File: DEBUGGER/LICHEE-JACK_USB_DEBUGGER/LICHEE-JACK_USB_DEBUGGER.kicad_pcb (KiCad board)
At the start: 2 copper layers, 45 x 20 mm, 52 parts, among them Q1 AO3401A, U1 USB2422/MJ, U3 TPSPX3819M5-L-3-3, U4 CP2102-GMR, X1 XL7EL89CMI-111YLC-24M

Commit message: replace some obj
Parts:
- removed LED3: LED_ORANGE/YELLOW_TXD, YLED0603O:LED0603-FD
- added LED5: LED_YELLOW_RXD, YLED0603G:LED0603-FD, F.Cu at (145.0, 63.0)
- added TP4: TP_VBUS, TestPoint:TestPoint_Pad_D1.0mm, B.Cu at (144.6, 71.2)
- added TP5: TP_GND, TestPoint:TestPoint_Pad_D1.0mm, B.Cu at (147.3, 71.2)
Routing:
- net GNDREF: track 153.9 -> 157.6 mm
- net VBUS: track 66.3 -> 68.3 mm

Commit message: rename LED5
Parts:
- renumbered LED5 to LED3
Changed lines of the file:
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@@
 	(net 58 "GNDREF")
 	(net 59 "Net-(D8-Pad2)")
-	(net 60 "Net-(LED5--)")
+	(net 60 "Net-(LED3--)")
 	(footprint "Capacitor_SMD:C_0402_1005Metric"
 		(layer "F.Cu")
@@
 			(layers "F.Cu" "F.Mask" "F.Paste")
 			(roundrect_rratio 0.25)
-			(net 60 "Net-(LED5--)")
+			(net 60 "Net-(LED3--)")
 			(pintype "passive")
 		)
@@
 		(layer "F.Cu")
 		(at 145 63 90)
-		(property "Reference" "LED5"
+		(property "Reference" "LED3"
 			(at 0 -4 90)
 			(layer "F.SilkS")
@@
 			(size 1 0.9)
 			(layers "F.Cu" "F.Mask" "F.Paste")
-			(net 60 "Net-(LED5--)")
+			(net 60 "Net-(LED3--)")
 			(pinfunction "-")
 			(pintype "unspecified")

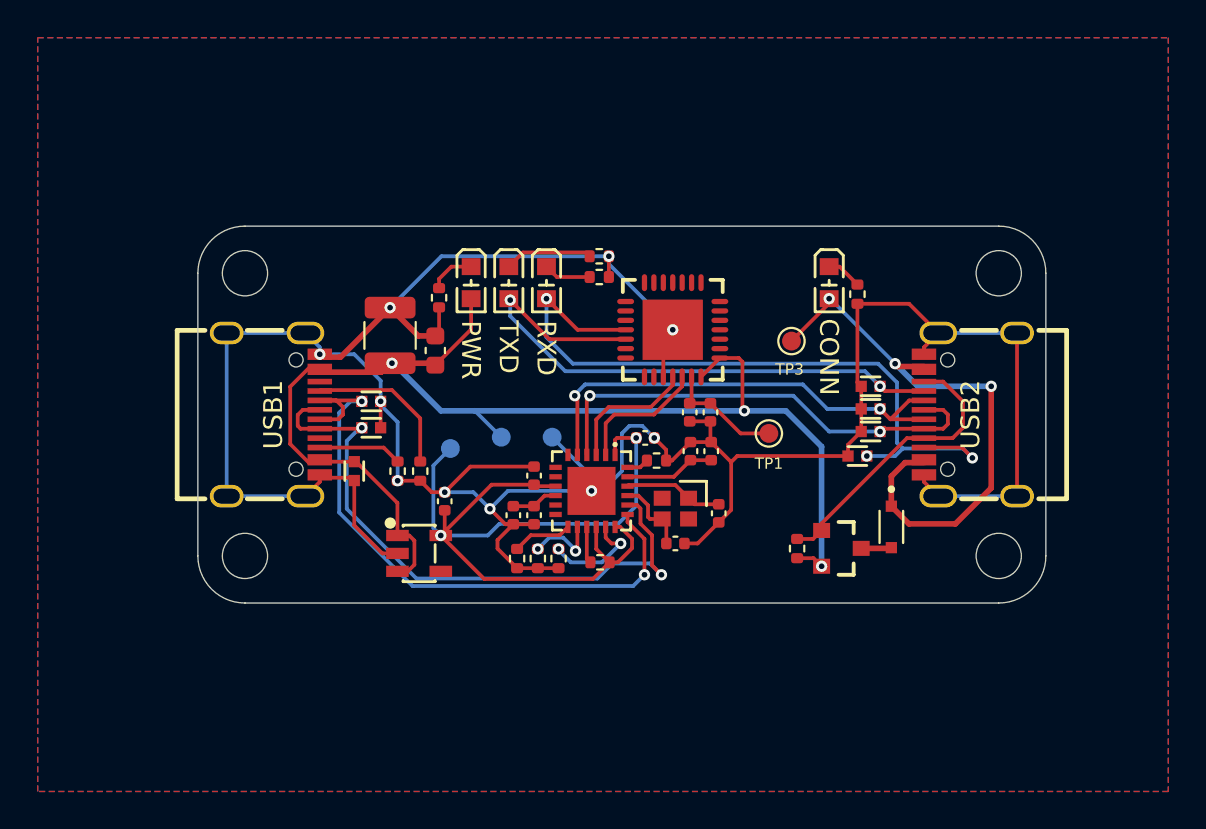
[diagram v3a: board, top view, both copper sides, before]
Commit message: fix TX/RX LED, USB DEBUGGER v1.1
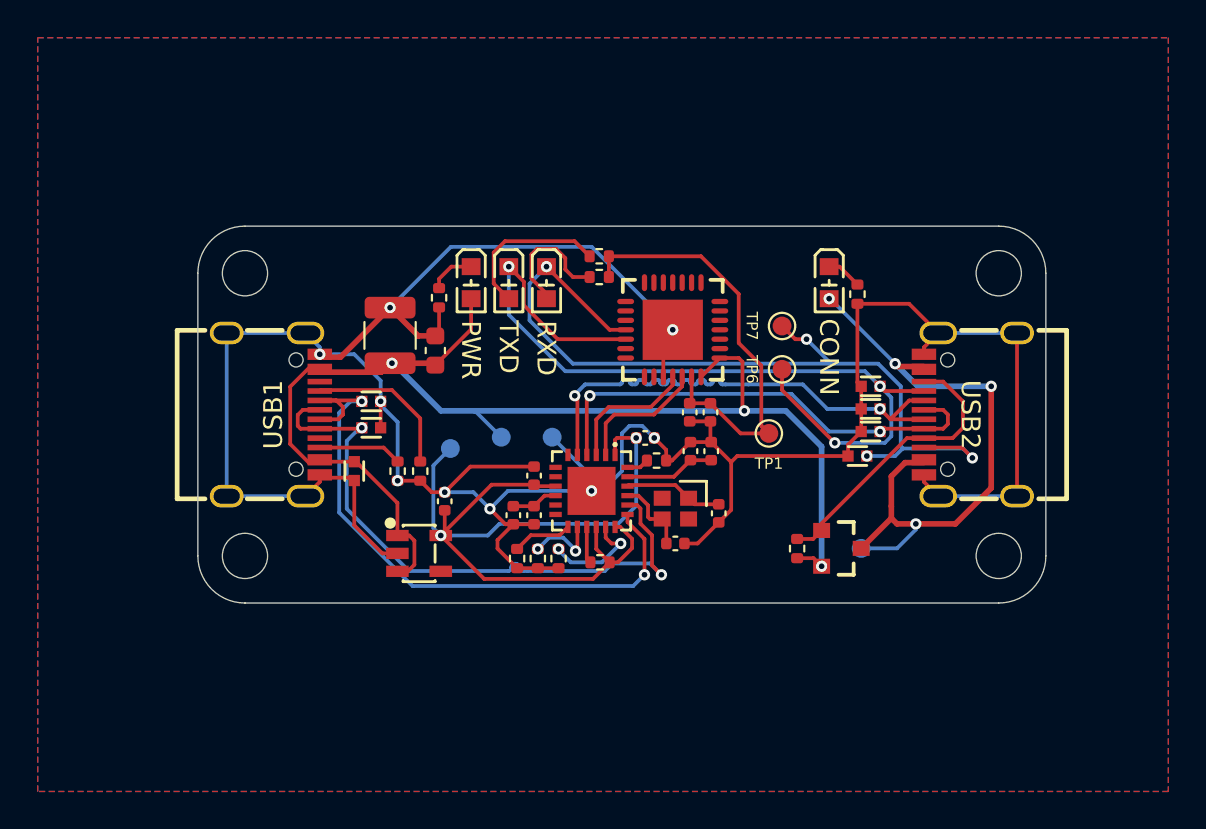
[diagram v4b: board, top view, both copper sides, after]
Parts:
- removed D8: SS1X-323, PMEG4010CEJ_115:DIO_PMEG4010CEJ_115
- added G***: LOGO, ICON:kali_3x3, B.Cu at (155.1, 66.4)
- added TP6: TP_TXD, TestPoint:TestPoint_Pad_D1.0mm, F.Cu at (159.5, 67.6)
- added TP7: TP_RXD, TestPoint:TestPoint_Pad_D1.0mm, F.Cu at (159.5, 65.3)
- G***: footprint UUID:e6e3c969-ea9f-4b59-9f61-3c9483aae457 -> UUID:23694cda-5ace-4d6f-9775-43e1d7cdbd87
- LED3: value LED_YELLOW_RXD -> LED_YELLOW_TXD
- TP3: moved to B.Cu
- moved TP3 11.6 mm to (163.7, 77.1), turned to 180 degrees
- moved G*** 0.30 mm to (151.8, 66.3)
- moved G*** 0.20 mm to (148.8, 66.2)
- moved G*** 0.10 mm to (145.2, 66.3)
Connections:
- net DN1_DM renamed DN1_DN
- net DN2_DM renamed DN2_DN
- C12 pad 2: TP_CP2102_VDD -> V3V3_CP2102
- C13 pad 2: TP_CP2102_VDD -> V3V3_CP2102
- LED3 pad 1: TXD -> Net-(LED3-+)
- LED3 pad 2: Net-(LED3--) -> TXD
- LED4 pad 1: RXD -> Net-(LED4-+)
- LED4 pad 2: Net-(LED4--) -> RXD
- Q1 pad 3: Net-(D8-Pad2) -> VCON
- R10 pad 1: Net-(LED3--) -> Net-(LED3-+)
- R10 pad 2: GNDREF -> V3V3_CP2102
- R9 pad 1: Net-(LED4--) -> Net-(LED4-+)
- R9 pad 2: GNDREF -> V3V3_CP2102
- TP1 pad 1: TP_CP2102_VDD -> V3V3_CP2102
- U4 pad 6: TP_CP2102_VDD -> V3V3_CP2102
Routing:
- net V3V3_CP2102: track 0.00 -> 23.2 mm
- net TXD: track 31.5 -> 45.9 mm, vias 2 -> 3
- net Net-(LED3-+): track 0.00 -> 8.56 mm
- net Net-(LED4-+): track 0.00 -> 6.87 mm
- net RXD: track 38.9 -> 45.5 mm, vias 3 -> 4
- net TP_CP2102_VDD: track 6.30 -> 0.00 mm
- net Net-(LED3--): track 4.68 -> 0.00 mm
- net VCON: track 30.7 -> 34.1 mm, vias 3 -> 4
- net Net-(LED4--): track 2.52 -> 0.00 mm
- net DN2_DP: track 25.0 -> 26.8 mm
- net Net-(D8-Pad2): track 1.62 -> 0.00 mm
- net GNDREF: track 157.6 -> 156.7 mm, vias 10 -> 9
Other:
- board text added: "23694cda-5ace-4d6f-9775-43e1d7cdbd87"
- board text added: "Lichee-Jack USB Debugger V1.1"
- board text added: "󱨊DEVICE󱨊"
- board text added: "󱨊HOST󱨊"
- board text removed: "Lichee-Jack USB Debugger V1.0"
- board text removed: "^DEVICE^"
- board text removed: "^HOST^"
- board text removed: "e6e3c969-ea9f-4b59-9f61-3c9483aae457"
